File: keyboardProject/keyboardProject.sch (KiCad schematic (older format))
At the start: 4 parts

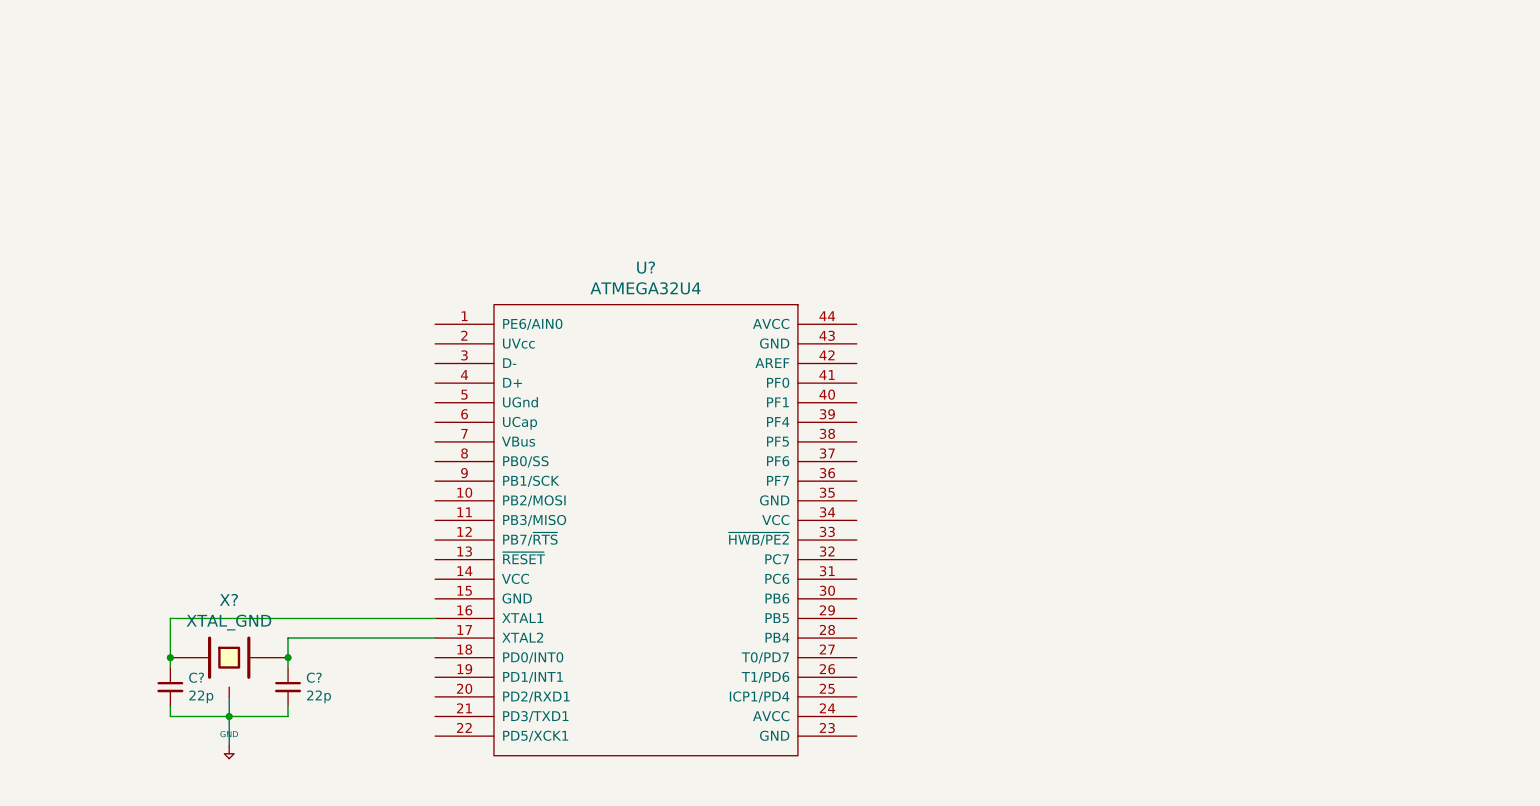
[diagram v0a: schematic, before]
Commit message: basic flashable microcontroller schematic
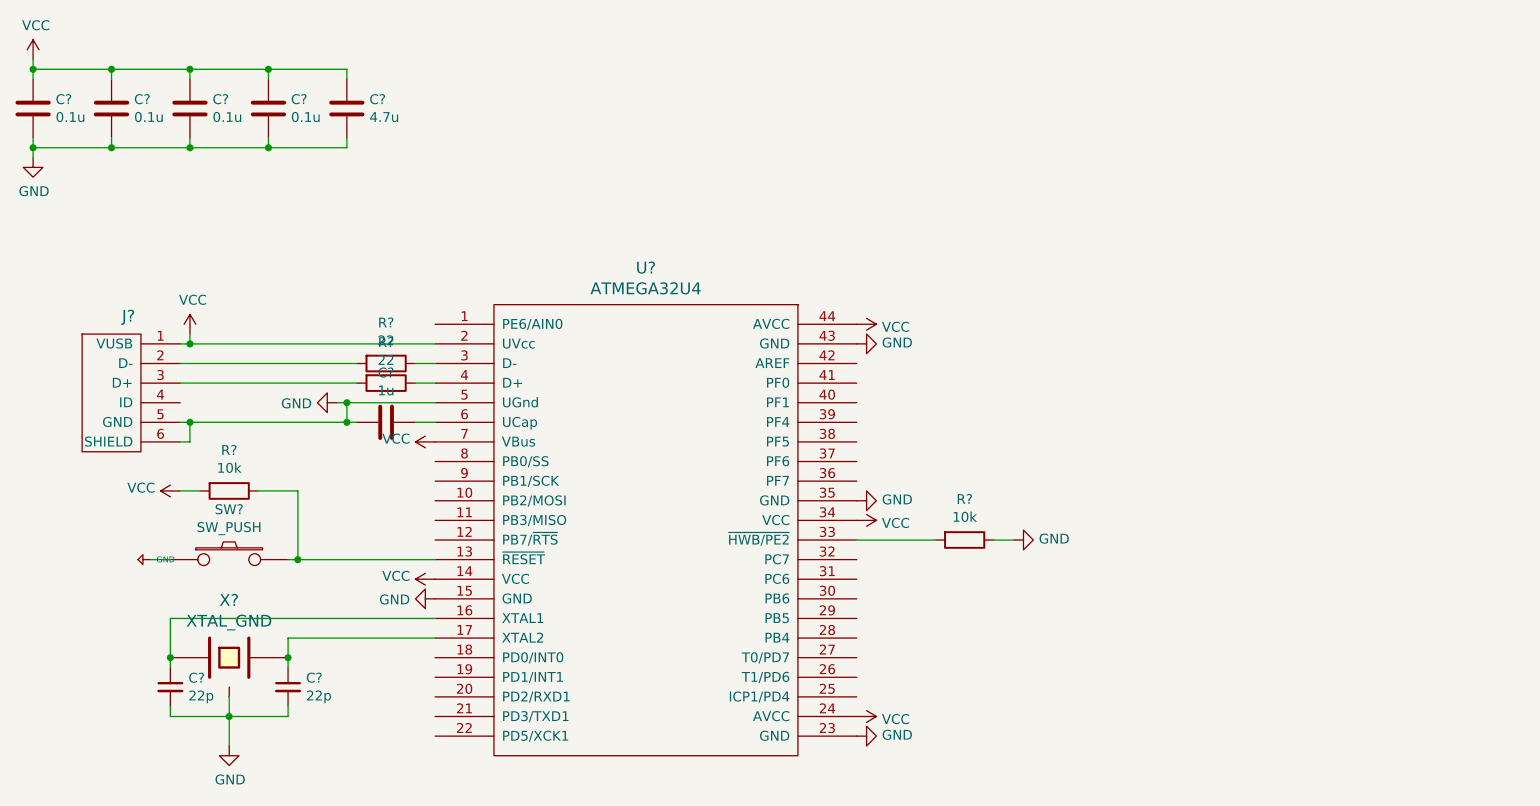
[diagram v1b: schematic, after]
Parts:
- added C? (x4): 0.1u, symbol Device:C
- added C?: 4.7u, symbol Device:C
- added C?: 1u, symbol Device:C
- added J?: USB_mini_micro_B, symbol keyboardParts:USB_mini_micro_B
- added R? (x2): 10k, symbol Device:R
- added R? (x2): 22, symbol Device:R
- added SW?: SW_PUSH, symbol keyboardParts:SW_PUSH
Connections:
- net +5V: now also SW?.1; no longer C?.2, C?.2, X?.3
- net at U?.13 (~RESET): now also R?.1, SW?.2
- net VCC: now reaches U?.14 (VCC)
- net VCC: now also U?.2 (UVcc), U?.24 (AVCC), U?.34 (VCC), U?.44 (AVCC), U?.7 (VBus), C?.1, C?.1, C?.1, C?.1, C?.1, J?.1 (VUSB), R?.2
- net GND: now reaches U?.15 (GND)
- net GND: now also C?.2, C?.2, U?.23 (GND), U?.35 (GND), U?.43 (GND), U?.5 (UGnd), X?.3, C?.2, C?.2, C?.2, C?.2, C?.2, C?.2, J?.5 (GND), J?.6 (SHIELD), R?.1
- net at U?.3 (D-): now also R?.1
- net at U?.33 (~HWB/PE2): now also R?.2
- net at U?.4 (D+): now also R?.1
- net at U?.6 (UCap): now also C?.1
- new net: J?.2 (D-), R?.2
- new net: J?.3 (D+), R?.2

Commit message: add 2x2 switch matrix
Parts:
- added D1, D2, D3, D4: D, symbol Device:D
- added K1, K2, K3, K4: KEYSW, symbol keyboardParts:KEYSW
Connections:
- new net: D1.2 (A), K1.2
- new net: D2.2 (A), K2.2
- new net: D3.2 (A), K3.2
- new net: D4.2 (A), K4.2
- new net col0: K1.1, K2.1
- new net col1: K3.1, K4.1
- new net row0: D1.1 (K), D3.1 (K)
- new net row1: D2.1 (K), D4.1 (K)
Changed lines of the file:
@@
 	0    -1   -1   0
 $EndComp
+$Comp
+L keyboardParts:KEYSW K1
+U 1 1 5F2A99A8
+P 7500 1850
+F 0 "K1" H 7500 2083 60  0000 C CNN
+F 1 "KEYSW" H 7500 1750 60  0001 C CNN
+F 2 "" H 7500 1850 60  0000 C CNN
+F 3 "" H 7500 1850 60  0000 C CNN
+	1    7500 1850
+	1    0    0    -1
+$EndComp
+$Comp
+L Device:D D1
+U 1 1 5F2AFAE4
+P 7150 2050
+F 0 "D1" V 7196 1970 50  0000 R CNN
+F 1 "D" V 7105 1970 50  0000 R CNN
+F 2 "" H 7150 2050 50  0001 C CNN
+F 3 "~" H 7150 2050 50  0001 C CNN
+	1    7150 2050
+	0    -1   -1   0
+$EndComp
+Wire Wire Line
+	7200 1850 7150 1850
+Wire Wire Line
+	7150 1850 7150 1900
+$Comp
+L keyboardParts:KEYSW K2
+U 1 1 5F2B9779
+P 7500 2750
+F 0 "K2" H 7500 2983 60  0000 C CNN
+F 1 "KEYSW" H 7500 2650 60  0001 C CNN
+F 2 "" H 7500 2750 60  0000 C CNN
+F 3 "" H 7500 2750 60  0000 C CNN
+	1    7500 2750
+	1    0    0    -1
+$EndComp
+$Comp
+L Device:D D2
+U 1 1 5F2B977F
+P 7150 2950
+F 0 "D2" V 7196 2870 50  0000 R CNN
+F 1 "D" V 7105 2870 50  0000 R CNN
+F 2 "" H 7150 2950 50  0001 C CNN
+F 3 "~" H 7150 2950 50  0001 C CNN
+	1    7150 2950
+	0    -1   -1   0
+$EndComp
+Wire Wire Line
+	7200 2750 7150 2750
+Wire Wire Line
+	7150 2750 7150 2800
+$Comp
+L keyboardParts:KEYSW K3
+U 1 1 5F2BF003
+P 8650 1850
+F 0 "K3" H 8650 2083 60  0000 C CNN
+F 1 "KEYSW" H 8650 1750 60  0001 C CNN
+F 2 "" H 8650 1850 60  0000 C CNN
+F 3 "" H 8650 1850 60  0000 C CNN
+	1    8650 1850
+	1    0    0    -1
+$EndComp
+$Comp
+L Device:D D3
+U 1 1 5F2BF009
+P 8300 2050
+F 0 "D3" V 8346 1970 50  0000 R CNN
+F 1 "D" V 8255 1970 50  0000 R CNN
+F 2 "" H 8300 2050 50  0001 C CNN
+F 3 "~" H 8300 2050 50  0001 C CNN
+	1    8300 2050
+	0    -1   -1   0
+$EndComp
+Wire Wire Line
+	8350 1850 8300 1850
+Wire Wire Line
+	8300 1850 8300 1900
+$Comp
+L keyboardParts:KEYSW K4
+U 1 1 5F2BF011
+P 8650 2750
+F 0 "K4" H 8650 2983 60  0000 C CNN
+F 1 "KEYSW" H 8650 2650 60  0001 C CNN
+F 2 "" H 8650 2750 60  0000 C CNN
+F 3 "" H 8650 2750 60  0000 C CNN
+	1    8650 2750
+	1    0    0    -1
+$EndComp
+$Comp
+L Device:D D4
+U 1 1 5F2BF017
+P 8300 2950
+F 0 "D4" V 8346 2870 50  0000 R CNN
+F 1 "D" V 8255 2870 50  0000 R CNN
+F 2 "" H 8300 2950 50  0001 C CNN
+F 3 "~" H 8300 2950 50  0001 C CNN
+	1    8300 2950
+	0    -1   -1   0
+$EndComp
+Wire Wire Line
+	8350 2750 8300 2750
+Wire Wire Line
+	8300 2750 8300 2800
+Wire Wire Line
+	8300 3100 7150 3100
+Wire Wire Line
+	8300 2200 7150 2200
+Wire Wire Line
+	7800 1850 7800 2750
+Wire Wire Line
+	8950 1850 8950 2750
+Text GLabel 7100 3100 0    50   Input ~ 0
+row1
+Wire Wire Line
+	7150 3100 7100 3100
+Connection ~ 7150 3100
+Text GLabel 7100 2200 0    50   Input ~ 0
+row0
+Wire Wire Line
+	7150 2200 7100 2200
+Connection ~ 7150 2200
+Text GLabel 7800 1700 1    50   Input ~ 0
+col0
+Wire Wire Line
+	7800 1700 7800 1850
+Connection ~ 7800 1850
+Text GLabel 8950 1700 1    50   Input ~ 0
+col1
+Wire Wire Line
+	8950 1700 8950 1850
+Connection ~ 8950 1850
 $EndSCHEMATC
